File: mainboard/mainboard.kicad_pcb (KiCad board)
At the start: 2 copper layers, 110 x 90 mm, 81 parts, among them K1 G6S-2F-5DC, X1 POWER, X10 BUTTONS, X2 IO, X3 INPUT, X4 FRONT INPUT, X5 MAIN OUTPUT, X6 PHONES OUTPUT, X7 UART, X8 DISPLAY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

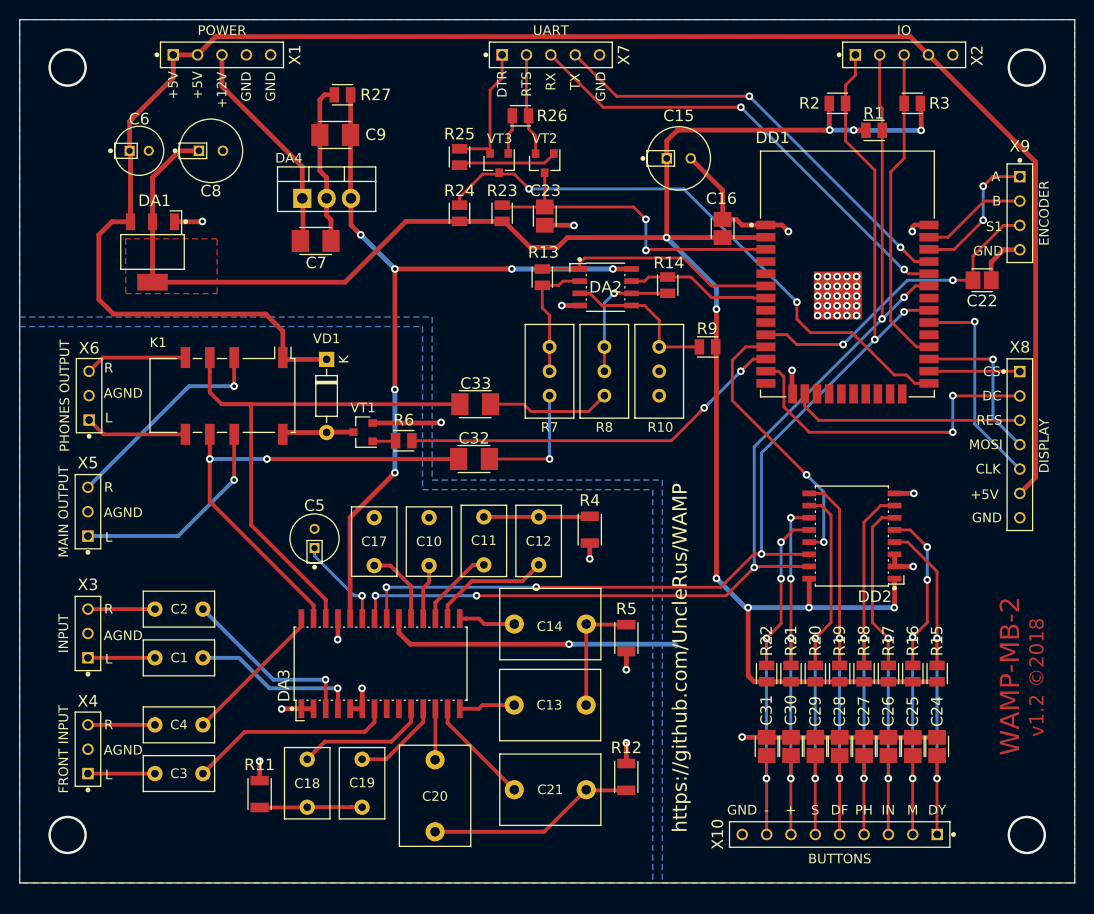
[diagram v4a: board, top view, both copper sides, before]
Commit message: Headphone amp added, minor MB fixes
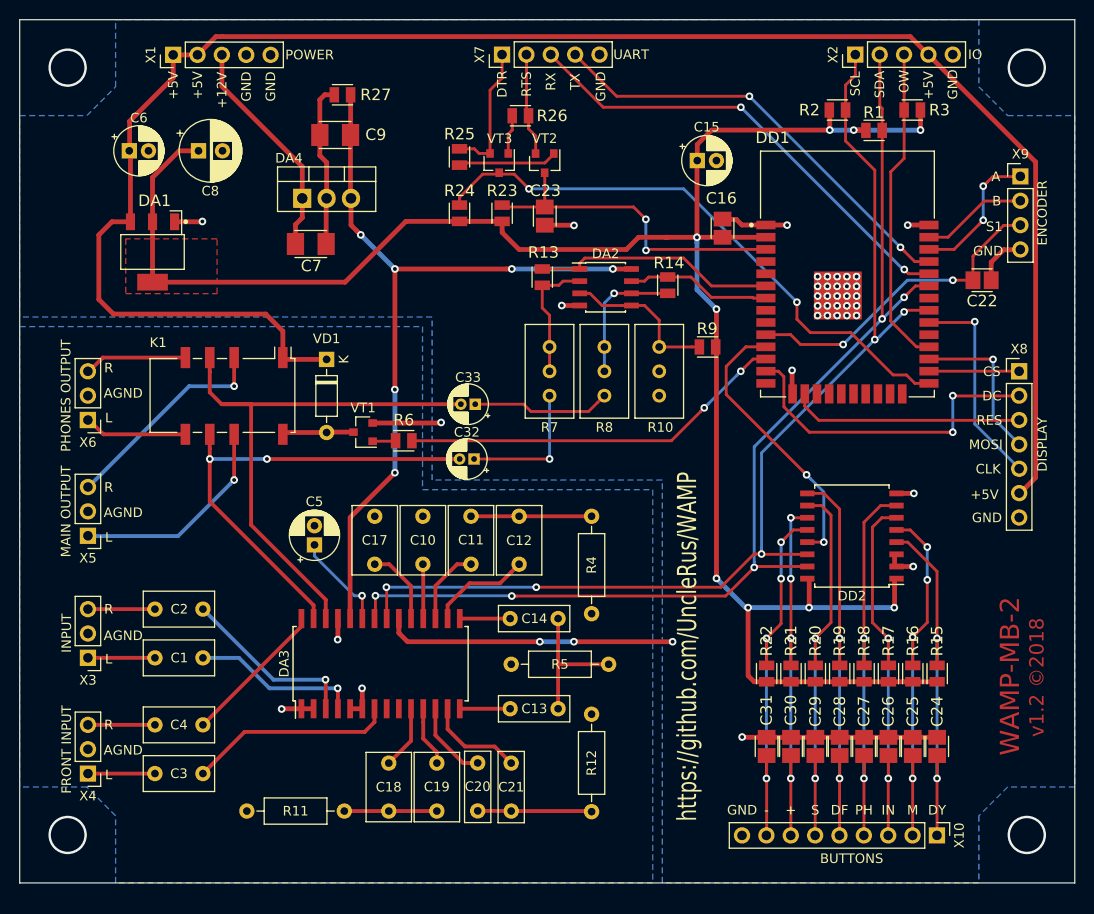
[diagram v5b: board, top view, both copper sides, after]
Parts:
- C11, C12, C18, C19: footprint Capacitor_THT:C_Rect_L7.2mm_W4.5mm_P5.00mm_FKS2_FKP2_MKS2_MKP2 -> Capacitor_THT:C_Rect_L7.0mm_W4.5mm_P5.00mm
- C13, C14, C20, C21: footprint Capacitor_THT:C_Rect_L10.3mm_W7.2mm_P7.50mm_MKS4 -> Capacitor_THT:C_Rect_L7.2mm_W2.5mm_P5.00mm_FKS2_FKP2_MKS2_MKP2
- C15: footprint WAMP:CAPPRD250W50D650H1300N -> Capacitor_THT:CP_Radial_D5.0mm_P2.00mm
- C32, C33: footprint WAMP:CAPC3216X180N -> Capacitor_THT:CP_Radial_D4.0mm_P1.50mm
- C5, C6: footprint WAMP:CAPPRD200W45D500H800N -> Capacitor_THT:CP_Radial_D5.0mm_P2.00mm
- C8: footprint WAMP:CAPPRD250W50D650H1300N -> Capacitor_THT:CP_Radial_D6.3mm_P2.50mm
- DA2: footprint WAMP:SOIC127P600X175-8N -> Package_SO:SOIC-8_3.9x4.9mm_P1.27mm
- DA3: footprint WAMP:SOIC127P1030X265-28N -> Package_SO:SOIC-28W_7.5x17.9mm_P1.27mm
- DD2: footprint WAMP:SOIC127P940X245-16N -> Package_SO:SOIC-16W_7.5x10.3mm_P1.27mm
- R11, R12, R4, R5: footprint WAMP:RESC3115X65N -> Resistor_THT:R_Axial_DIN0207_L6.3mm_D2.5mm_P10.16mm_Horizontal
- X1, X2, X7: footprint WAMP:CON_CONN_BL_05X01 -> Connector_PinHeader_2.54mm:PinHeader_1x05_P2.54mm_Vertical
- X10: footprint WAMP:CON_CONN_BL_09X01 -> Connector_PinHeader_2.54mm:PinHeader_1x09_P2.54mm_Vertical
- X3, X4, X5, X6: footprint WAMP:CON_CONN_BL_03X01 -> Connector_PinHeader_2.54mm:PinHeader_1x03_P2.54mm_Vertical
- X8: footprint WAMP:CON_CONN_BL_07X01 -> Connector_PinHeader_2.54mm:PinHeader_1x07_P2.54mm_Vertical
- X9: footprint WAMP:CON_CONN_BL_04X01 -> Connector_PinHeader_2.54mm:PinHeader_1x04_P2.54mm_Vertical
- moved R5 12.3 mm to (138.3, 103.0), turned to 0 degrees
- moved X10 10.1 mm to (182.7, 120.9)
- moved R11 9.00 mm to (120.9, 118.3)
- moved R4 8.77 mm to (146.7, 97.7), turned to 90 degrees
- moved C18 8.51 mm to (125.5, 118.3)
- moved C21 8.14 mm to (138.3, 118.3), turned to 90 degrees
- moved C19 7.81 mm to (130.5, 118.3)
- moved X8 7.65 mm to (191.2, 72.5)
- moved R12 5.12 mm to (146.7, 118.4), turned to 90 degrees
- moved X7 5.09 mm to (137.3, 39.4)
- moved X2 5.09 mm to (174.2, 39.4)
- moved X1 5.09 mm to (103.0, 39.5)
- moved C20 4.95 mm to (134.8, 118.3)
- moved X9 3.84 mm to (191.4, 52.1)
- moved C14 2.99 mm to (143.2, 98.2)
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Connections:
- C32 pad 1: /LOUT -> Net-(C32-Pad1)
- C32 pad 2: Net-(C32-Pad2) -> /LOUT
- C33 pad 1: /ROUT -> Net-(C33-Pad1)
- C33 pad 2: Net-(C33-Pad2) -> /ROUT
- R7 pad 1: Net-(C32-Pad2) -> Net-(C32-Pad1)
- R8 pad 1: Net-(C33-Pad2) -> Net-(C33-Pad1)
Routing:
- net Net-(C32-Pad1): track 0.00 -> 14.5 mm, vias 0 -> 1
- net Net-(C33-Pad1): track 0.00 -> 14.5 mm
- net Net-(C32-Pad2): track 12.9 -> 0.00 mm, vias 1 -> 0
- net Net-(C33-Pad2): track 12.9 -> 0.00 mm
- net Net-(C20-Pad1): track 21.8 -> 11.9 mm
- net GND: track 113.8 -> 105.2 mm, vias 36 -> 38
- net AGND: track 16.7 -> 8.95 mm, vias 7 -> 3
- net /MIN_R: track 13.8 -> 6.63 mm
- net +3V3: track 221.1 -> 214.7 mm
- net /MOUT_R: track 9.37 -> 6.26 mm
- net /BIN_R: track 5.34 -> 8.37 mm
- net Net-(C13-Pad1): track 12.7 -> 14.7 mm
- net /MOUT_L: track 12.6 -> 10.6 mm
- net Net-(C11-Pad1): track 11.1 -> 12.6 mm
- net /BOUT_R: track 11.3 -> 10.2 mm
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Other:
- board text added: "OW"
- board text added: "SCL"
- board text added: "SDA"

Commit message: v1.3
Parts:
- added C34: 100n, WAMP:CAPC2013X140N, F.Cu at (44.2, 74.4)
- added REF**: OSHW-Symbol_8.9x8mm_SilkScreen, Symbol:OSHW-Symbol_8.9x8mm_SilkScreen, F.Cu at (55.3, 91.5)
- added REF**: MountingHole_2.7mm_M2.5_DIN965, MountingHole:MountingHole_2.7mm_M2.5_DIN965, F.Cu at (126.1, 68.6)
- added REF**: MountingHole_2.7mm_M2.5_DIN965, MountingHole:MountingHole_2.7mm_M2.5_DIN965, F.Cu at (-12.9, 112.6)
- added REF**: MountingHole_2.7mm_M2.5_DIN965, MountingHole:MountingHole_2.7mm_M2.5_DIN965, F.Cu at (-12.9, 68.6)
- DA4: footprint Package_TO_SOT_THT:TO-220-3_Vertical -> Package_TO_SOT_SMD:TO-263-2
- VD1: footprint Diode_THT:D_DO-35_SOD27_P7.62mm_Horizontal -> Diode_SMD:D_MiniMELF
- X1: footprint Connector_PinHeader_2.54mm:PinHeader_1x05_P2.54mm_Vertical -> Connector_PinHeader_2.54mm:PinHeader_1x07_P2.54mm_Vertical
- X8: footprint Connector_PinHeader_2.54mm:PinHeader_1x07_P2.54mm_Vertical -> Connector_PinHeader_2.54mm:PinHeader_1x08_P2.54mm_Vertical
- moved X7 122.4 mm to (39.1, 112.5)
- moved R12 115.7 mm to (31.1, 112.7)
- moved R4 115.7 mm to (31.1, 92.0)
- moved R5 115.7 mm to (22.7, 97.3)
- moved C13 115.7 mm to (27.6, 101.9)
- moved C14 115.7 mm to (27.6, 92.5)
- moved DA3 115.7 mm to (9.09, 97.2)
- moved R26 114.4 mm to (42.5, 106.9), turned to 270 degrees
- moved VT2 114.0 mm to (39.9, 102.0), turned to 90 degrees
- moved C11 112.7 mm to (21.6, 81.9)
- moved C12 112.7 mm to (26.6, 81.9)
- moved C17 112.7 mm to (11.5, 81.9)
- moved C10 112.7 mm to (16.5, 81.9)
- moved C5 112.4 mm to (5.50, 85.6)
- moved C18 111.8 mm to (13.8, 112.6)
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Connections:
- C7 pad 1: Net-(C7-Pad1) -> /12V
- DA4 pad 1: Net-(C7-Pad1) -> /12V
- X1 pad 1: +5V -> AGND
- X1 pad 2: +5V -> AGND
- X1 pad 3: Net-(C7-Pad1) -> GND
- X1 pad 5: GND -> +5V
- X8 pad 7: GND -> +3V3
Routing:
- net GND: track 105.2 -> 47.5 mm, vias 38 -> 154
- net /PH_SW: track 40.4 -> 81.6 mm, vias 2 -> 6
- net /LOUT: track 49.6 -> 87.0 mm, vias 2 -> 3
- net /SDA: track 114.3 -> 147.1 mm, vias 5 -> 7
- net /SCL: track 114.4 -> 145.4 mm, vias 5 -> 8
- net /ROUT: track 58.7 -> 85.2 mm, vias 0 -> 3
- net Net-(C7-Pad1): track 23.5 -> 0.00 mm
- net +3V3: track 214.7 -> 191.6 mm, vias 9 -> 42
- net /TXD: track 45.8 -> 68.6 mm, vias 2 -> 1
- net /RE_BTN: track 33.5 -> 56.1 mm
- net /RXD: track 48.9 -> 69.9 mm
- net /EN: track 34.7 -> 52.8 mm
- net /RE_B: track 11.0 -> 28.7 mm
- net Net-(C3-Pad2): track 21.5 -> 5.12 mm
- net Net-(C1-Pad1): track 6.98 -> 21.7 mm
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- added copper zone on B.Cu, net +3V3
- added copper zone on F.Cu, net AGND
- added copper zone on F.Cu, net GND
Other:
- board size 110 x 90 mm -> 145 x 50 mm
- board text added: "+3V3"
- board text added: "FRONT IN"
- board text added: "G"
- board text added: "H.PH. OUT"
- board text added: "MAIN IN"
- board text added: "MAIN OUT"
- board text added: "v1.3 ©2018"
- board text removed: "https://github.com/UncleRus/WAMP"
- board text removed: "v1.2 ©2018"

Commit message: Firmware started
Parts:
- moved R5 2.47 mm to (20.2, 97.3)
- moved C13 1.85 mm to (25.7, 101.9)
- moved C14 1.85 mm to (25.7, 92.5)
- moved C12 1.61 mm to (25.6, 83.1)
- moved R4 1.51 mm to (30.1, 93.2)
- moved C11 1.50 mm to (20.7, 83.1)
- moved C10 1.40 mm to (15.9, 83.1)
- moved C21 1.36 mm to (25.6, 111.7)
- moved C17 1.33 mm to (11.1, 83.1)
- moved R12 1.32 mm to (30.1, 111.7)
- moved C1 1.22 mm to (0.05, 83.1)
- moved C4 1.16 mm to (-3.38, 95.7)
- moved C2 1.15 mm to (-3.38, 98.8)
- moved C20 1.06 mm to (22.5, 111.7)
- moved C5 1.05 mm to (5.76, 86.6)
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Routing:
- net GND: track 47.5 -> 56.2 mm, vias 154 -> 129
- net +3V3: track 191.6 -> 194.0 mm
- net +9V: track 90.8 -> 93.0 mm
- net /BOUT_L: track 5.25 -> 3.40 mm
- net /BIN_L: track 5.25 -> 3.40 mm
- net Net-(C1-Pad1): track 21.7 -> 19.9 mm
- net /LOUT: track 87.0 -> 85.5 mm
- net /MOUT_L: track 13.7 -> 12.1 mm
- net /TREB_L: track 6.92 -> 5.40 mm
- net Net-(DA2-Pad3): track 20.0 -> 18.5 mm
- net Net-(C4-Pad2): track 6.46 -> 5.00 mm
- net /BOUT_R: track 13.7 -> 12.3 mm
- net /MIN_L: track 9.93 -> 8.59 mm
- net Net-(C13-Pad1): track 14.7 -> 13.3 mm
- net Net-(C1-Pad2): track 16.9 -> 15.7 mm
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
